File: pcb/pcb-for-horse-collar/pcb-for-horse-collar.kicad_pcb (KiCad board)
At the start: 2 copper layers, 24 parts, among them J1 Conn_01x02_Socket, P1 USB_C_Plug_USB2.0, Q1 S8050, Q2 S8050, U1 ESP32-WROOM-32E, U2 BNO085, U3 CP2102N-Axx-xQFN28, U4 MCP73831-2-OT, U5 AP2112K-3.3

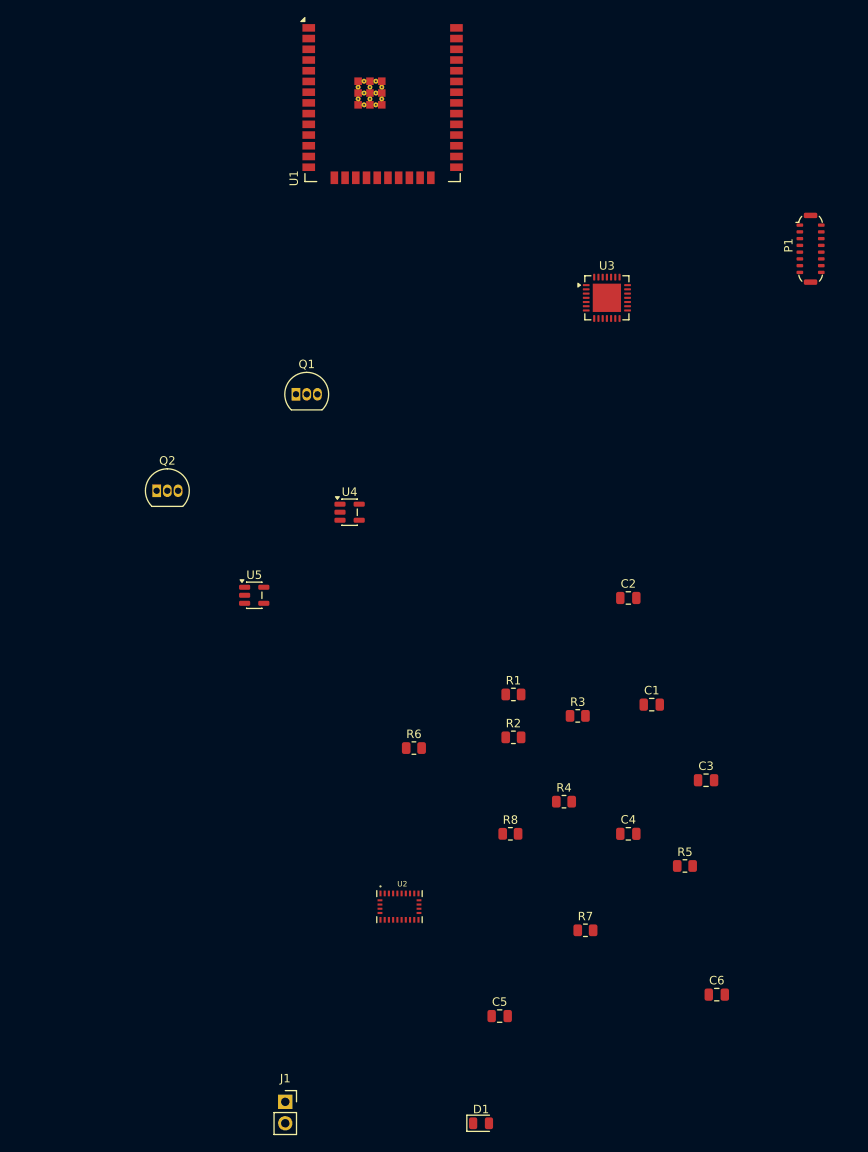
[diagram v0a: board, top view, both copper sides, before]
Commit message: WIP: About to add mosfet for charging and switch to turn it on and off.
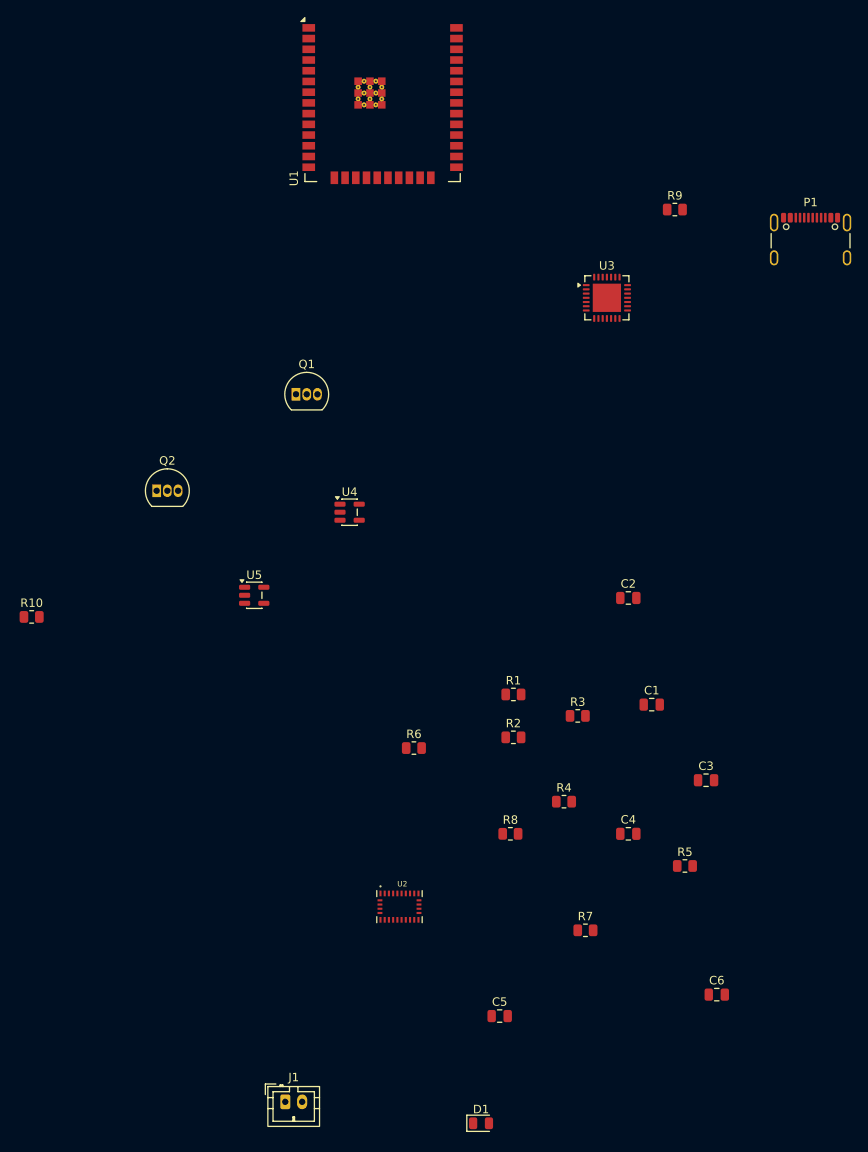
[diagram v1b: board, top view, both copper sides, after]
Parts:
- added R10: 5.1 kΩ, Resistor_SMD:R_0805_2012Metric, F.Cu at (79.2, 105.1)
- added R9: 10 kΩ, Resistor_SMD:R_0805_2012Metric, F.Cu at (155.4, 56.9)
- J1: footprint Connector_PinSocket_2.54mm:PinSocket_1x02_P2.54mm_Vertical -> Connector_JST:JST_PH_B2B-PH-K_1x02_P2.00mm_Vertical
- P1: value USB_C_Plug_USB2.0 -> USB_C_Receptacle_USB2.0_16P; footprint Connector_USB:USB_C_Plug_ShenzhenJingTuoJin_918-118A2021Y40002_Vertical -> Connector_USB:USB_C_Receptacle_GCT_USB4105-xx-A_16P_TopMnt_Horizontal
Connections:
- D1 pad 2: Net-(D1-A) -> /VBUS
- P1 pad A8: (no net) -> unconnected-(P1-SBU1-PadA8)
- P1 pad B5: unconnected-(P1-VCONN-PadB5) -> Net-(P1-CC2)
- P1 pad B6: (no net) -> unconnected-(P1-D+-PadB6)
- P1 pad B7: (no net) -> unconnected-(P1-D--PadB7)
- P1 pad B8: (no net) -> unconnected-(P1-SBU2-PadB8)
- R2 pad 1: Net-(D1-A) -> Net-(U4-STAT)
- R2 pad 2: /VBUS -> Net-(D1-K)
- R4 pad 1: /BNO_H_SCL -> /3V3
- R4 pad 2: /3V3 -> /BNO_H_SCL
- U2 pad 10: unconnected-(U2-CLKSEL0-Pad10) -> GND
- U2 pad 4: unconnected-(U2-~{BOOT}-Pad4) -> Net-(U2-~{BOOT})
- U4 pad 1: Net-(D1-K) -> Net-(U4-STAT)

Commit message: Adding switch.
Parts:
- added SW1: SW_SPST, Button_Switch_SMD:SW_DIP_SPSTx01_Slide_6.7x4.1mm_W6.73mm_P2.54mm_LowProfile_JPin, F.Cu at (89.0, 138.4)
